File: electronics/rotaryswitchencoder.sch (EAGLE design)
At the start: 13 parts, among them IC1 74HC14N

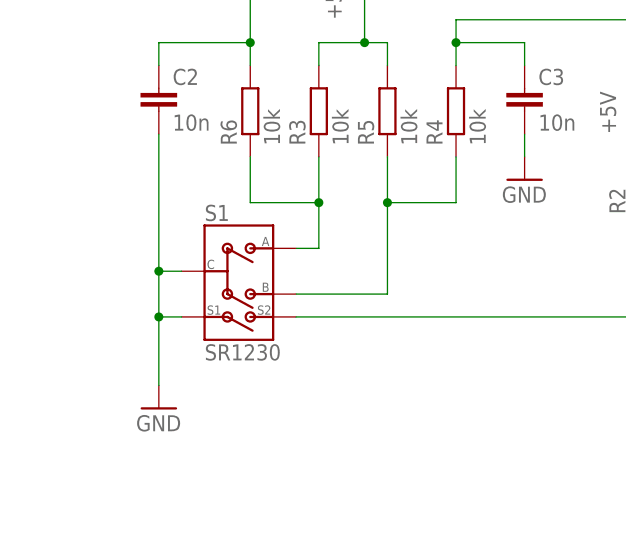
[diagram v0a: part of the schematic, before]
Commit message: Switched out cables. Created circuit board for switch.
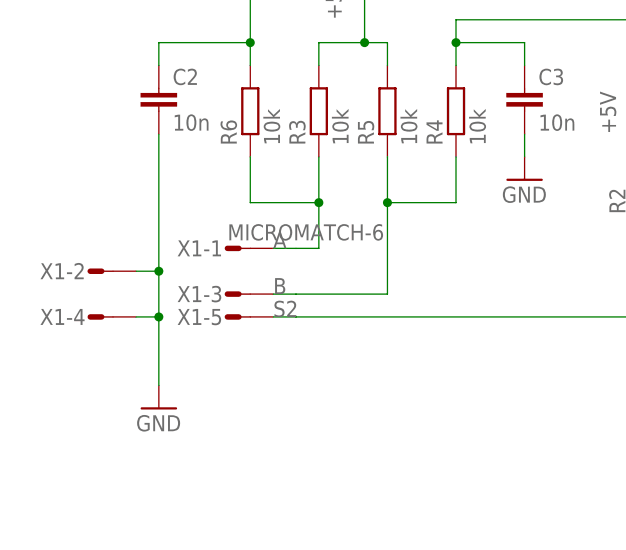
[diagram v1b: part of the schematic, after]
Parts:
- removed S1: SR1230, rotaryencoderswitch:SR1230
- added X1: MICROMATCH-6, con-amp-micromatch:MICROMATCH-6
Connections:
- removed net N$1: D1.A, R1.1, R2.1, S1.S2
- removed net N$4: R3.1, R6.1, S1.A
- removed net N$5: R4.1, R5.1, S1.B
- new net A: R3.1, R6.1, X1-1.S
- new net B: R4.1, R5.1, X1-3.S
- new net S2: D1.A, R1.1, R2.1, X1-5.S
- net GND: now also X1-2.S, X1-4.S; no longer S1.C, S1.S1
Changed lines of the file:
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@@
 <part name="R2" library="resistor" library_urn="urn:adsk.eagle:library:348" deviceset="R-EU_" device="0204/7" package3d_urn="urn:adsk.eagle:package:23498/1" value="10k"/>
 <part name="D1" library="diode" library_urn="urn:adsk.eagle:library:210" deviceset="1N4148" device="DO35-7" package3d_urn="urn:adsk.eagle:package:43339/1"/>
-<part name="S1" library="rotaryencoderswitch" deviceset="SR1230" device="" value="SR1230"/>
 <part name="R3" library="resistor" library_urn="urn:adsk.eagle:library:348" deviceset="R-EU_" device="0204/7" package3d_urn="urn:adsk.eagle:package:23498/1" value="10k"/>
 <part name="R4" library="resistor" library_urn="urn:adsk.eagle:library:348" deviceset="R-EU_" device="0204/7" package3d_urn="urn:adsk.eagle:package:23498/1" value="10k"/>
@@
 <part name="C4" library="rcl" library_urn="urn:adsk.eagle:library:334" deviceset="C-EU" device="050-024X044" package3d_urn="urn:adsk.eagle:package:23643/1" value="0.1u"/>
 <part name="P+3" library="supply1" library_urn="urn:adsk.eagle:library:371" deviceset="+5V" device=""/>
+<part name="X1" library="con-amp-micromatch" library_urn="urn:adsk.eagle:library:122" deviceset="MICROMATCH-6" device="" package3d_urn="urn:adsk.eagle:package:5703/1"/>
 </parts>
 <sheets>
@@
 <instance part="R2" gate="G$1" x="10.16" y="81.28" rot="R90"/>
 <instance part="D1" gate="G$1" x="17.78" y="73.66"/>
-<instance part="S1" gate="G$1" x="-38.1" y="76.2"/>
 <instance part="R3" gate="G$1" x="-25.4" y="88.9" rot="R90"/>
 <instance part="R4" gate="G$1" x="-10.16" y="88.9" rot="R90"/>
@@
 <instance part="C4" gate="G$1" x="60.96" y="58.42"/>
 <instance part="P+3" gate="1" x="45.72" y="81.28"/>
+<instance part="X1" gate="-1" x="-35.56" y="73.66"/>
+<instance part="X1" gate="-2" x="-50.8" y="71.12"/>
+<instance part="X1" gate="-3" x="-35.56" y="68.58"/>
+<instance part="X1" gate="-4" x="-50.8" y="66.04"/>
+<instance part="X1" gate="-5" x="-35.56" y="66.04"/>
 </instances>
 <busses>
 </busses>
 <nets>
-<net name="N$1" class="0">
+<net name="S2" class="0">
 <segment>
 <pinref part="R2" gate="G$1" pin="1"/>
@@
 <wire x1="10.16" y1="73.66" x2="15.24" y2="73.66" width="0.1524" layer="91"/>
 <junction x="10.16" y="73.66"/>
-<pinref part="S1" gate="G$1" pin="S2"/>
 <wire x1="-27.94" y1="66.04" x2="10.16" y2="66.04" width="0.1524" layer="91"/>
 <junction x="10.16" y="66.04"/>
+<pinref part="X1" gate="-5" pin="S"/>
+<wire x1="-30.48" y1="66.04" x2="-27.94" y2="66.04" width="0.1524" layer="91"/>
+<label x="-30.48" y="66.04" size="1.778" layer="95"/>
 </segment>
 </net>
@@
 </segment>
 </net>
-<net name="N$4" class="0">
+<net name="A" class="0">
 <segment>
-<pinref part="S1" gate="G$1" pin="A"/>
 <wire x1="-27.94" y1="73.66" x2="-25.4" y2="73.66" width="0.1524" layer="91"/>
 <pinref part="R3" gate="G$1" pin="1"/>
@@
 <wire x1="-33.02" y1="78.74" x2="-25.4" y2="78.74" width="0.1524" layer="91"/>
 <junction x="-25.4" y="78.74"/>
+<pinref part="X1" gate="-1" pin="S"/>
+<wire x1="-30.48" y1="73.66" x2="-27.94" y2="73.66" width="0.1524" layer="91"/>
+<label x="-30.48" y="73.66" size="1.778" layer="95"/>
 </segment>
 </net>
-<net name="N$5" class="0">
+<net name="B" class="0">
 <segment>
-<pinref part="S1" gate="G$1" pin="B"/>
 <wire x1="-27.94" y1="68.58" x2="-17.78" y2="68.58" width="0.1524" layer="91"/>
 <pinref part="R5" gate="G$1" pin="1"/>
@@
 <wire x1="-10.16" y1="78.74" x2="-17.78" y2="78.74" width="0.1524" layer="91"/>
 <junction x="-17.78" y="78.74"/>
+<pinref part="X1" gate="-3" pin="S"/>
+<wire x1="-30.48" y1="68.58" x2="-27.94" y2="68.58" width="0.1524" layer="91"/>
+<label x="-30.48" y="68.58" size="1.778" layer="95"/>
 </segment>
 </net>
 <net name="GND" class="0">
 <segment>
-<pinref part="S1" gate="G$1" pin="C"/>
-<wire x1="-40.64" y1="71.12" x2="-43.18" y2="71.12" width="0.1524" layer="91"/>
 <wire x1="-43.18" y1="71.12" x2="-43.18" y2="66.04" width="0.1524" layer="91"/>
-<pinref part="S1" gate="G$1" pin="S1"/>
-<wire x1="-43.18" y1="66.04" x2="-40.64" y2="66.04" width="0.1524" layer="91"/>
 <pinref part="GND1" gate="1" pin="GND"/>
 <wire x1="-43.18" y1="58.42" x2="-43.18" y2="66.04" width="0.1524" layer="91"/>
@@
 <pinref part="C2" gate="G$1" pin="2"/>
 <wire x1="-43.18" y1="86.36" x2="-43.18" y2="71.12" width="0.1524" layer="91"/>
+<pinref part="X1" gate="-2" pin="S"/>
+<wire x1="-45.72" y1="71.12" x2="-43.18" y2="71.12" width="0.1524" layer="91"/>
 <junction x="-43.18" y="71.12"/>
+<pinref part="X1" gate="-4" pin="S"/>
+<wire x1="-45.72" y1="66.04" x2="-43.18" y2="66.04" width="0.1524" layer="91"/>
 </segment>
 <segment>
